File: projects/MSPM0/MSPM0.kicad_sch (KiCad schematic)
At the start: 8 parts, among them U1 MSPM0G3507SPTR

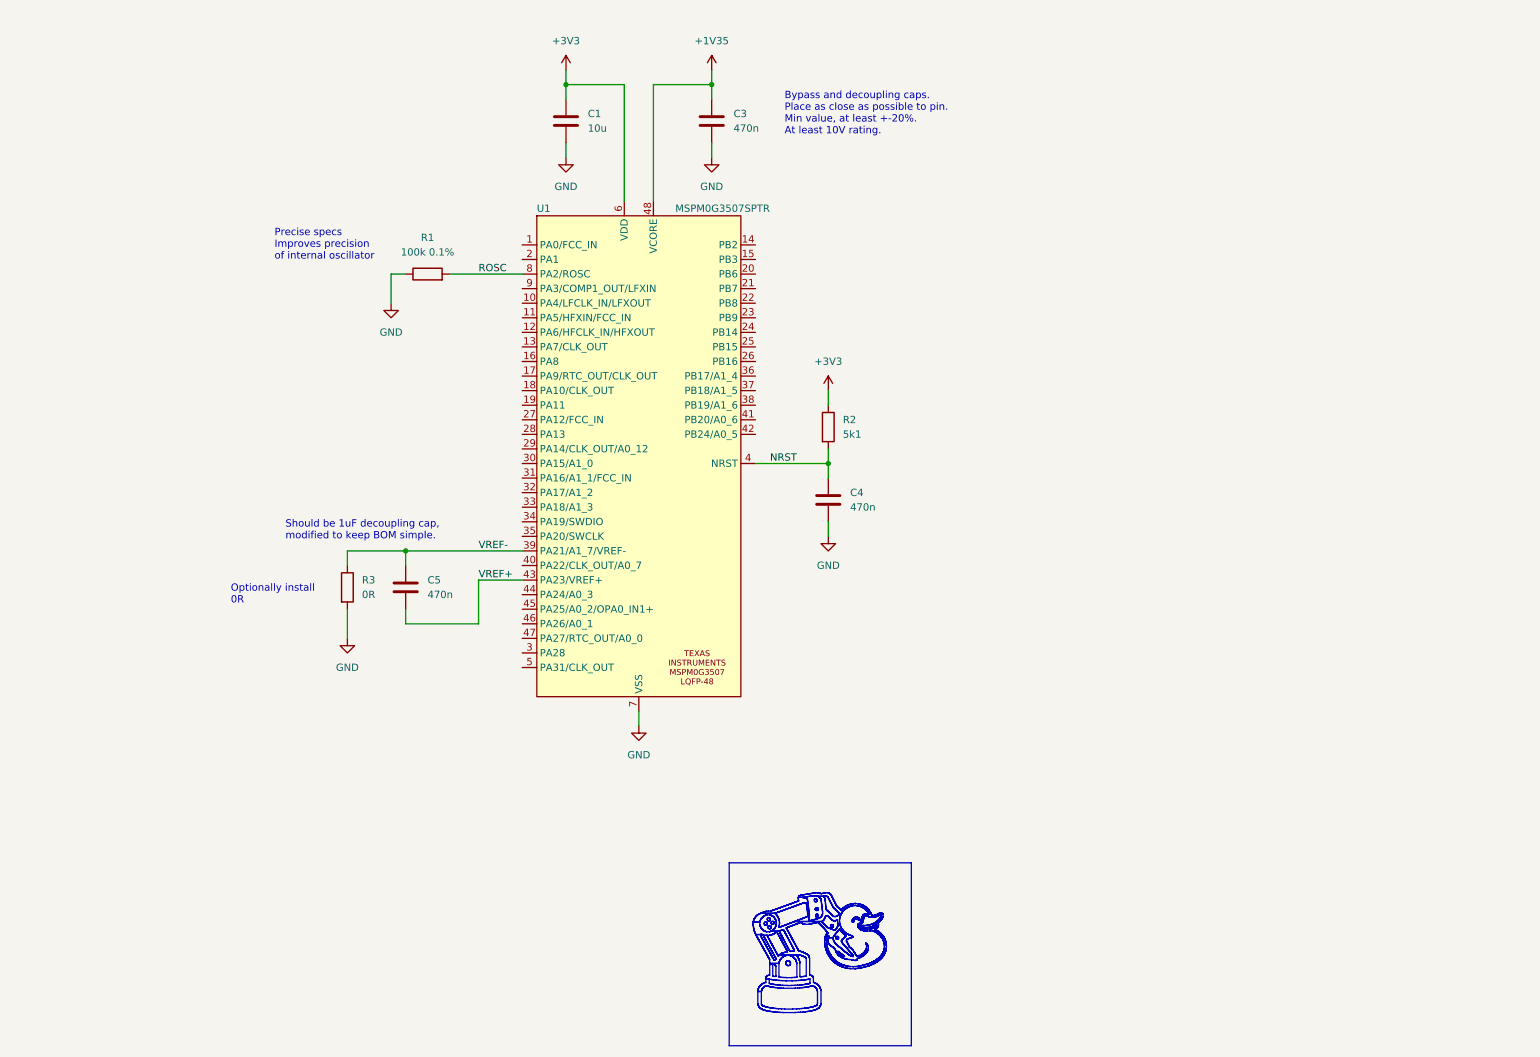
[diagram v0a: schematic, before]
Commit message: MSPM0 - schematics up to power rail
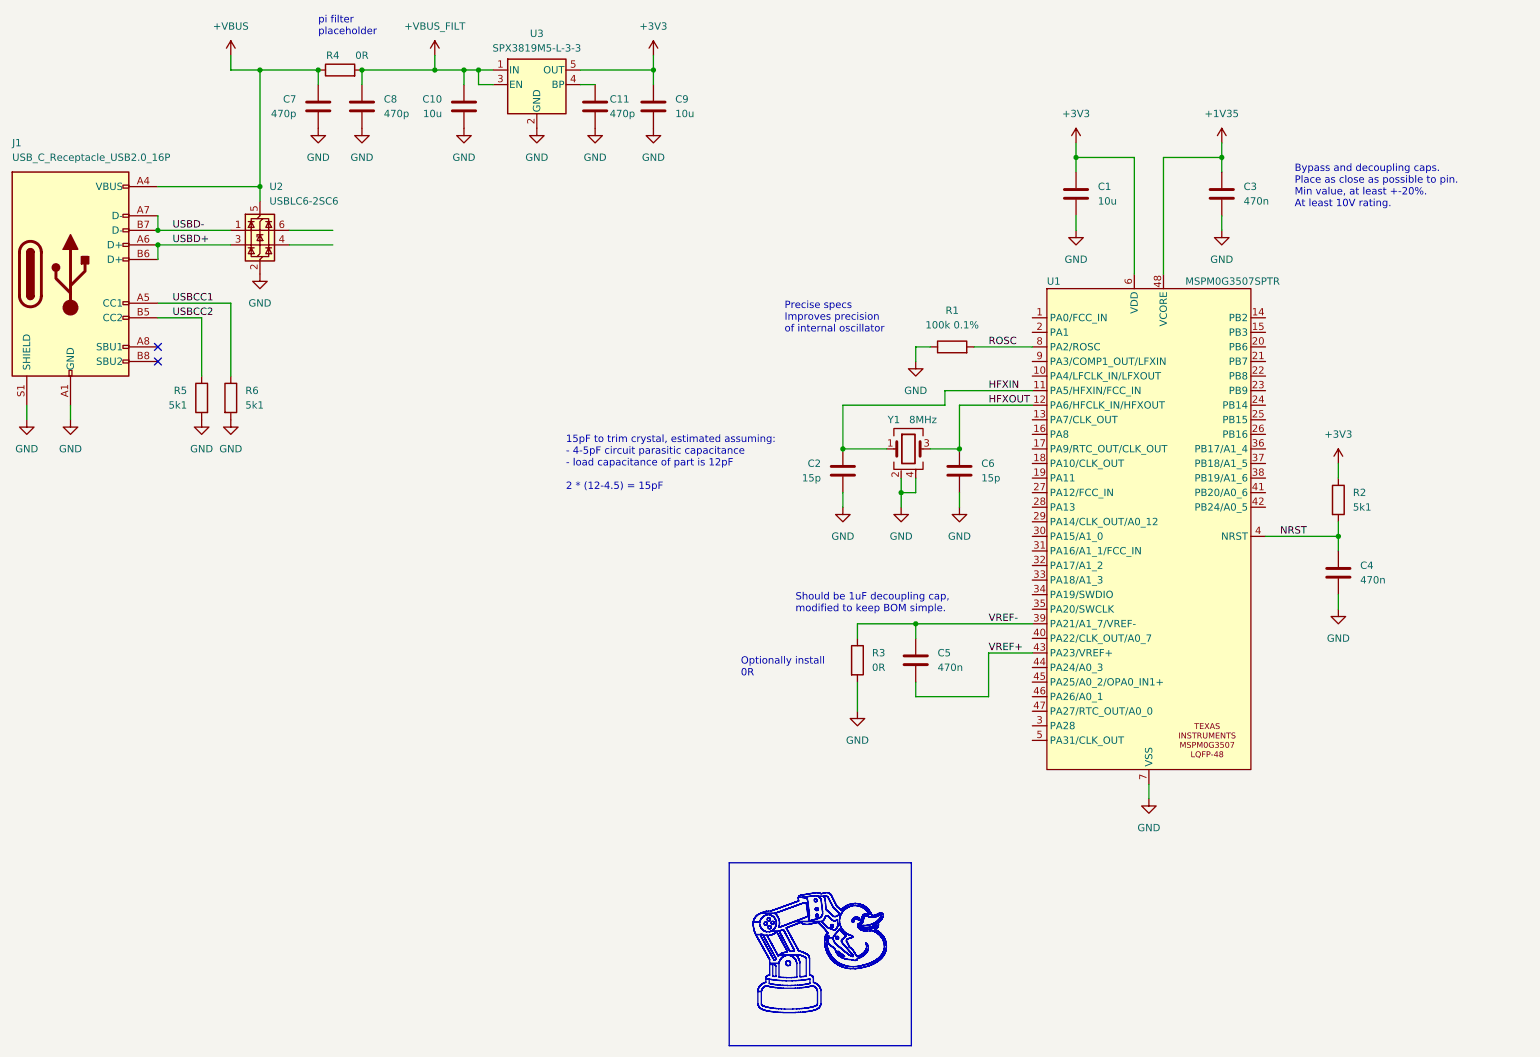
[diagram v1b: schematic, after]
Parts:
- added C10, C9: 10u, Capacitor_SMD:C_1206_3216Metric_Pad1.33x1.80mm_HandSolder, symbol MH_library:C
- added C11, C7, C8: 470p, Capacitor_SMD:C_1206_3216Metric_Pad1.33x1.80mm_HandSolder, symbol MH_library:C
- added C2, C6: 15p, Capacitor_SMD:C_1206_3216Metric_Pad1.33x1.80mm_HandSolder, symbol MH_library:C
- added J1: USB_C_Receptacle_USB2.0_16P, Connector_USB:USB_C_Receptacle_G-Switch_GT-USB-7010ASV, symbol MH_library:USB_C_Receptacle_USB2.0_16P
- added R4: 0R, Resistor_SMD:R_0201_0603Metric_Pad0.64x0.40mm_HandSolder, symbol MH_library:R
- added R5, R6: 5k1, Resistor_SMD:R_0201_0603Metric_Pad0.64x0.40mm_HandSolder, symbol MH_library:R
- added U2: USBLC6-2SC6, Package_TO_SOT_SMD:SOT-23-6, symbol MH_library:USBLC6-2SC6
- added U3: SPX3819M5-L-3-3, Package_TO_SOT_SMD:SOT-23-5, symbol MH_library:SPX3819M5-L-3-3
- added Y1: 8MHz, Crystal:Crystal_SMD_3225-4Pin_3.2x2.5mm, symbol MH_library:Crystal_GND24
- R1: LCSC C122538 -> (none); LCSC PN (none) -> C122538
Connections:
- net +3V3: now also C9.1, U3.5 (OUT)
- net GND: now also C10.2, C11.2, C2.2, C6.2, C7.2, C8.2, C9.2, J1.A1 (GND), J1.A12 (GND), J1.B1 (GND), J1.B12 (GND), J1.S1 (SHIELD), R5.2, R6.2, U2.2 (GND), U3.2 (GND), Y1.2 (G), Y1.4 (G)
- net HFXIN: now reaches U1.11 (PA5/HFXIN/FCC_IN)
- net HFXIN: now also C2.1, Y1.1
- net HFXOUT: now reaches U1.12 (PA6/HFCLK_IN/HFXOUT)
- net HFXOUT: now also C6.1, Y1.3
- new net: C11.1, U3.4 (BP)
- new net +VBUS: C7.1, J1.A4 (VBUS), J1.A9 (VBUS), J1.B4 (VBUS), J1.B9 (VBUS), R4.1, U2.5 (VBUS)
- new net +VBUS_FILT: C10.1, C8.1, R4.2, U3.1 (IN), U3.3 (EN)
- new net USBCC1: J1.A5 (CC1), R6.1
- new net USBCC2: J1.B5 (CC2), R5.1
- new net USBD+: J1.A6 (D+), J1.B6 (D+), U2.3 (I/O2)
- new net USBD-: J1.A7 (D-), J1.B7 (D-), U2.1 (I/O1)
- no-connect marks 0 -> 2
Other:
- note added: "15pF to trim crystal, estimated assuming: - 4-5pF circuit parasitic capacitance - load capacitance of part is 12pF 2 * (12-4.5) = 15pF"
- note added: "pi filter placeholder"
- moved on the sheet: C1, C3, C4, C5, R1, R2, R3, U1

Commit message: Add IMU and magnetometer (WIP)
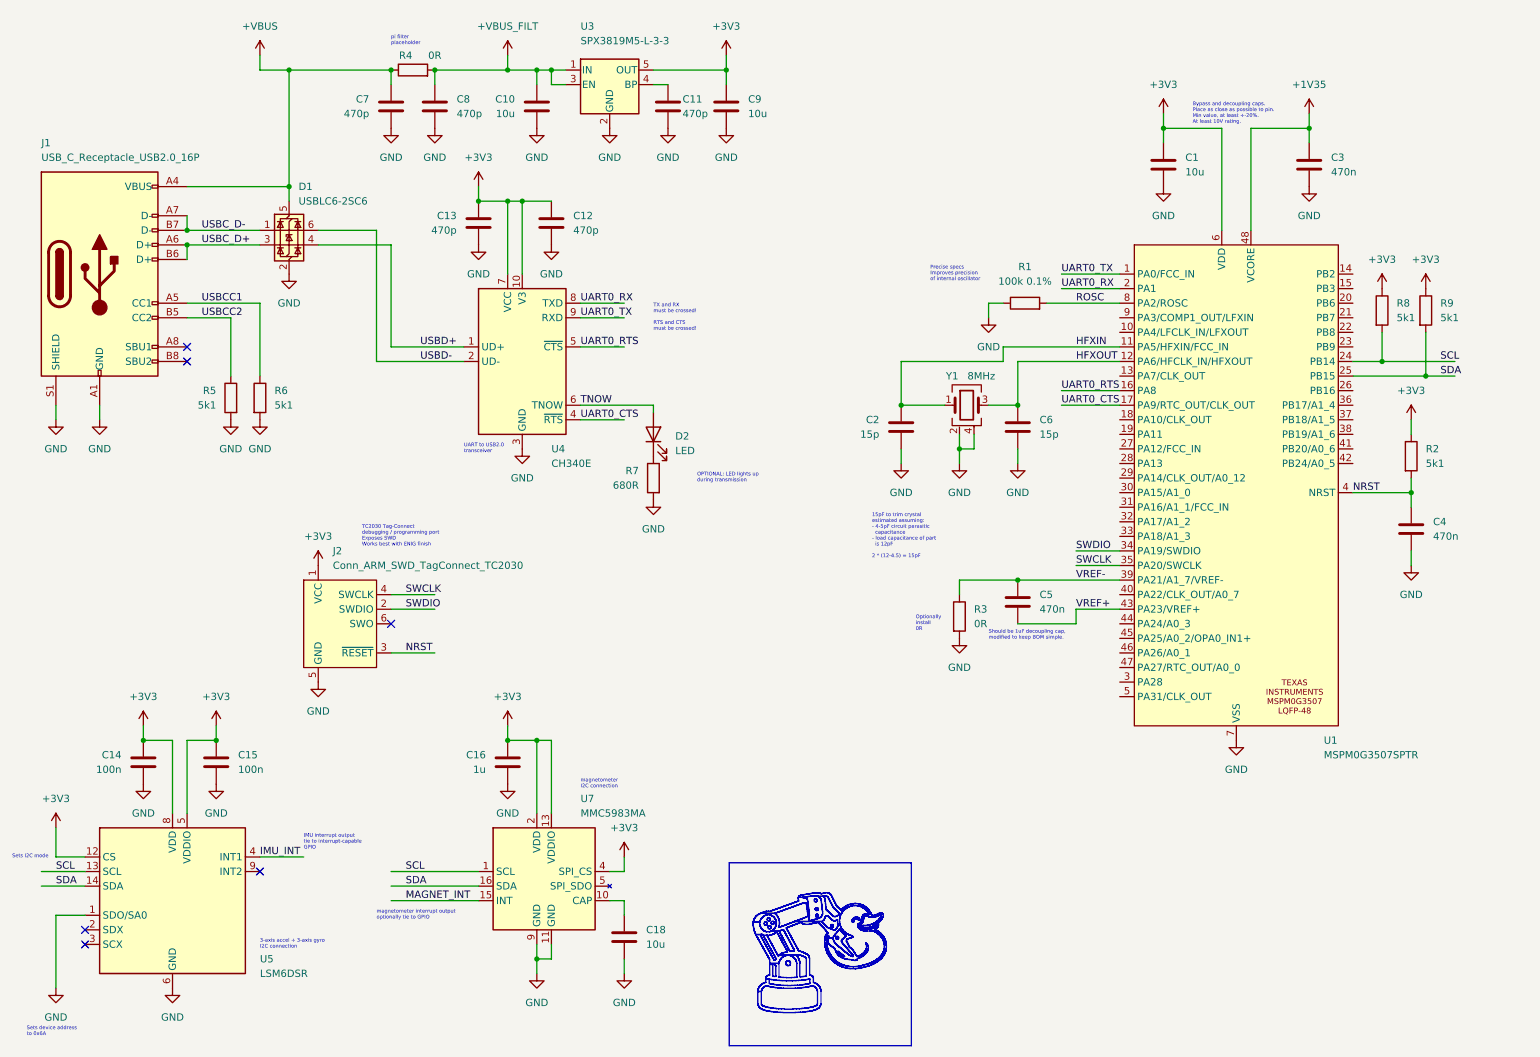
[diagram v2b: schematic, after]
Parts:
- removed U2: USBLC6-2SC6, Package_TO_SOT_SMD:SOT-23-6, symbol MH_library:USBLC6-2SC6
- added C12, C13: 470p, Capacitor_SMD:C_1206_3216Metric_Pad1.33x1.80mm_HandSolder, symbol MH_library:C
- added C14, C15: 100n, Capacitor_SMD:C_1206_3216Metric_Pad1.33x1.80mm_HandSolder, symbol MH_library:C
- added C16: 1u, Capacitor_SMD:C_1206_3216Metric_Pad1.33x1.80mm_HandSolder, symbol MH_library:C
- added C18: 10u, Capacitor_SMD:C_1206_3216Metric_Pad1.33x1.80mm_HandSolder, symbol MH_library:C
- added D1: USBLC6-2SC6, Package_TO_SOT_SMD:SOT-23-6, symbol MH_library:USBLC6-2SC6
- added D2: LED, LED_SMD:LED_1206_3216Metric_Pad1.42x1.75mm_HandSolder, symbol Device:LED
- added J2: Conn_ARM_SWD_TagConnect_TC2030, Connector:Tag-Connect_TC2030-IDC-FP_2x03_P1.27mm_Vertical, symbol MH_library:Conn_ARM_SWD_TagConnect_TC2030
- added R7: 680R, Resistor_SMD:R_0201_0603Metric_Pad0.64x0.40mm_HandSolder, symbol MH_library:R
- added R8, R9: 5k1, Resistor_SMD:R_0201_0603Metric_Pad0.64x0.40mm_HandSolder, symbol MH_library:R
- added U4: CH340E, Package_SO:MSOP-10_3x3mm_P0.5mm, symbol Interface_USB:CH340E
- added U5: LSM6DSR, Package_LGA:LGA-14_3x2.5mm_P0.5mm_LayoutBorder3x4y, symbol MH_library:LSM6DSR
- added U7: MMC5983MA, Package_LGA:LGA-16_3x3mm_P0.5mm, symbol MH_library:MMC5983MA
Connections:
- net +3V3: now also C12.1, C13.1, C14.1, C15.1, C16.1, J2.1 (VCC), R8.1, R9.1, U4.10 (V3), U4.7 (VCC), U5.12 (CS), U5.5 (VDDIO), U5.8 (VDD), U7.13 (VDDIO), U7.2 (VDD), U7.4 (SPI_CS)
- net +VBUS: now also D1.5 (VBUS)
- net GND: now also C12.2, C13.2, C14.2, C15.2, C16.2, C18.2, D1.2 (GND), J2.5 (GND), R7.2, U4.3 (GND), U5.1 (SDO/SA0), U5.6 (GND), U5.7 (GND), U7.11 (GND), U7.9 (GND)
- net NRST: now also J2.3 (~{RESET})
- net USBD+: now also D1.4 (I/O2), U4.1 (UD+); no longer J1.A6 (D+), J1.B6 (D+)
- net USBD-: now also D1.6 (I/O1), U4.2 (UD-); no longer J1.A7 (D-), J1.B7 (D-)
- net UART0_TX: now reaches U1.1 (PA0/FCC_IN)
- net UART0_TX: now also U4.9 (RXD)
- net UART0_RTS: now reaches U1.16 (PA8)
- net UART0_RTS: now also U4.5 (~{CTS})
- net UART0_CTS: now reaches U1.17 (PA9/RTC_OUT/CLK_OUT)
- net UART0_CTS: now also U4.4 (~{RTS})
- net UART0_RX: now reaches U1.2 (PA1)
- net UART0_RX: now also U4.8 (TXD)
- net SCL: now reaches U1.24 (PB14)
- net SCL: now also R8.2, U5.13 (SCL), U7.1 (SCL)
- net SDA: now reaches U1.25 (PB15)
- net SDA: now also R9.2, U5.14 (SDA), U7.16 (SDA)
- net SWDIO: now reaches U1.34 (PA19/SWDIO)
- net SWDIO: now also J2.2 (SWDIO)
- net SWCLK: now reaches U1.35 (PA20/SWCLK)
- net SWCLK: now also J2.4 (SWCLK)
- new net: D2.1 (K), R7.1
- new net: C18.1, U7.10 (CAP)
- new net IMU_INT: U5.4 (INT1)
- new net MAGNET_INT: U7.15 (INT)
- new net TNOW: D2.2 (A), U4.6 (TNOW)
- new net USBC_D+: D1.3 (I/O2), J1.A6 (D+), J1.B6 (D+)
- new net USBC_D-: D1.1 (I/O1), J1.A7 (D-), J1.B7 (D-)
- no-connect marks 2 -> 6
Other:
- note added: "15pF to trim crystal estimated assuming: - 4-5pF circuit parasitic capacitance - load capacitance of part is 12pF 2 * (12-4.5) = 15pF"
- note added: "3-axis accel + 3-axis gyro I2C connection"
- note added: "IMU interrupt output tie to interrupt-capable GPIO"
- note added: "OPTIONAL: LED lights up during transmission"
- note added: "Sets I2C mode"
- note added: "Sets device address to 0x6A"
- note added: "TC2030 Tag-Connect debugging / programming port Exposes SWD Works best with ENIG finish"
- note added: "TX and RX must be crossed! RTS and CTS must be crossed!"
- note added: "UART to USB2.0 transceiver"
- note added: "magnetometer I2C connection"
- note added: "magnetometer interrupt output optionally tie to GPIO"
- note removed: "15pF to trim crystal, estimated assuming: - 4-5pF circuit parasitic capacitance - load capacitance of part is 12pF 2 * (12-4.5) = 15pF"
- moved on the sheet: C1, C10, C11, C2, C3, C4, C5, C6, C7, C8, C9, J1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
